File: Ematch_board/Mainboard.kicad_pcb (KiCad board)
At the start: 4 copper layers, 57 x 53 mm, 124 parts, among them J1 Conn_01x02_Male, J10 Conn_01x02_Male, J11 Conn_Coaxial, J2 Conn_01x02_Male, J3 Conn_01x02_Male, J4 Conn_01x02_Male, J5 Conn_01x02_Male, J6 Conn_01x02_Male, J7 RBUS, J8 USB_C_Receptacle_USB2.0, J9 Conn_01x02_Male, Q1 MMDT2222A, Q51 PMV20ENR, Q52 PMV20ENR, Q53 PMV20ENR, Q54 PMV20ENR, Q55 PMV20ENR, Q56 PMV20ENR, U1 LTV-247, U2 LTC4411, U3 SC4216H, U4 LTC4411, U5 SN65HVD230, U6 CP2102-GMR-QFN28

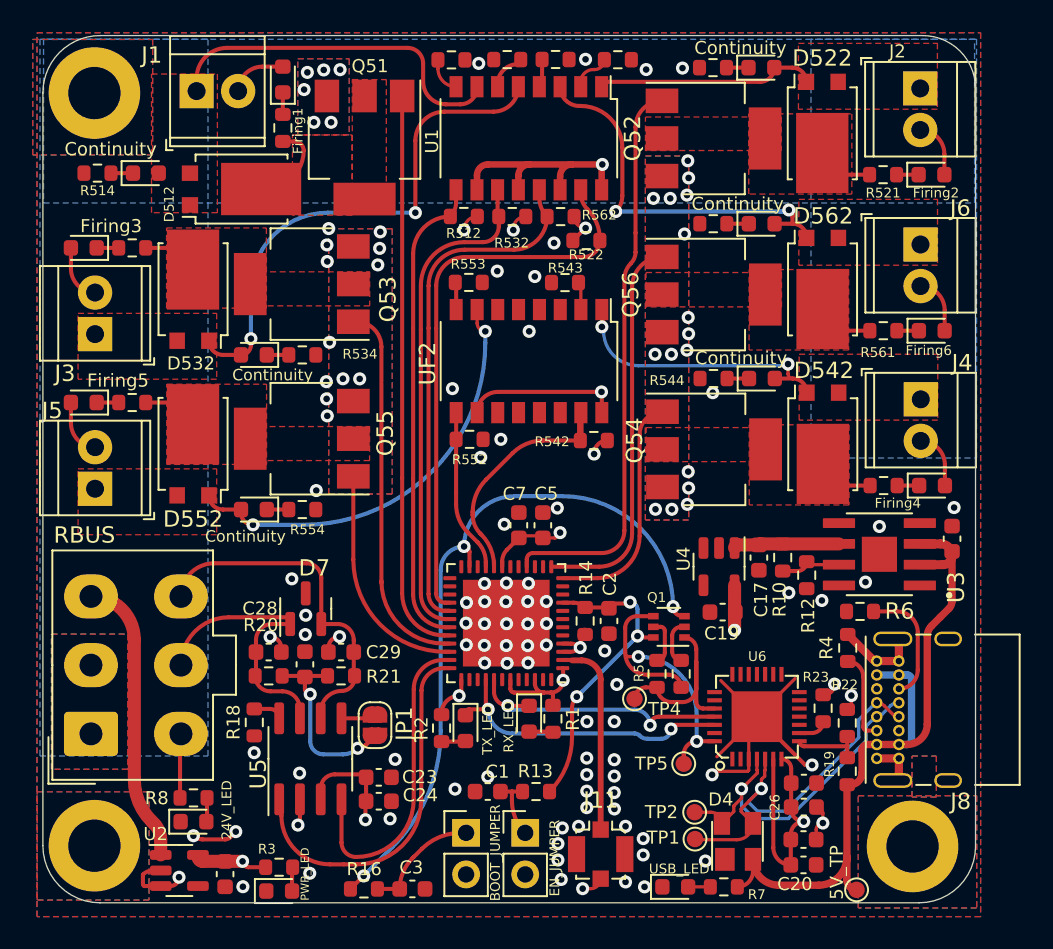
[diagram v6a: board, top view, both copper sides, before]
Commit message: Changed ESP32 pin assignment from special IO pins
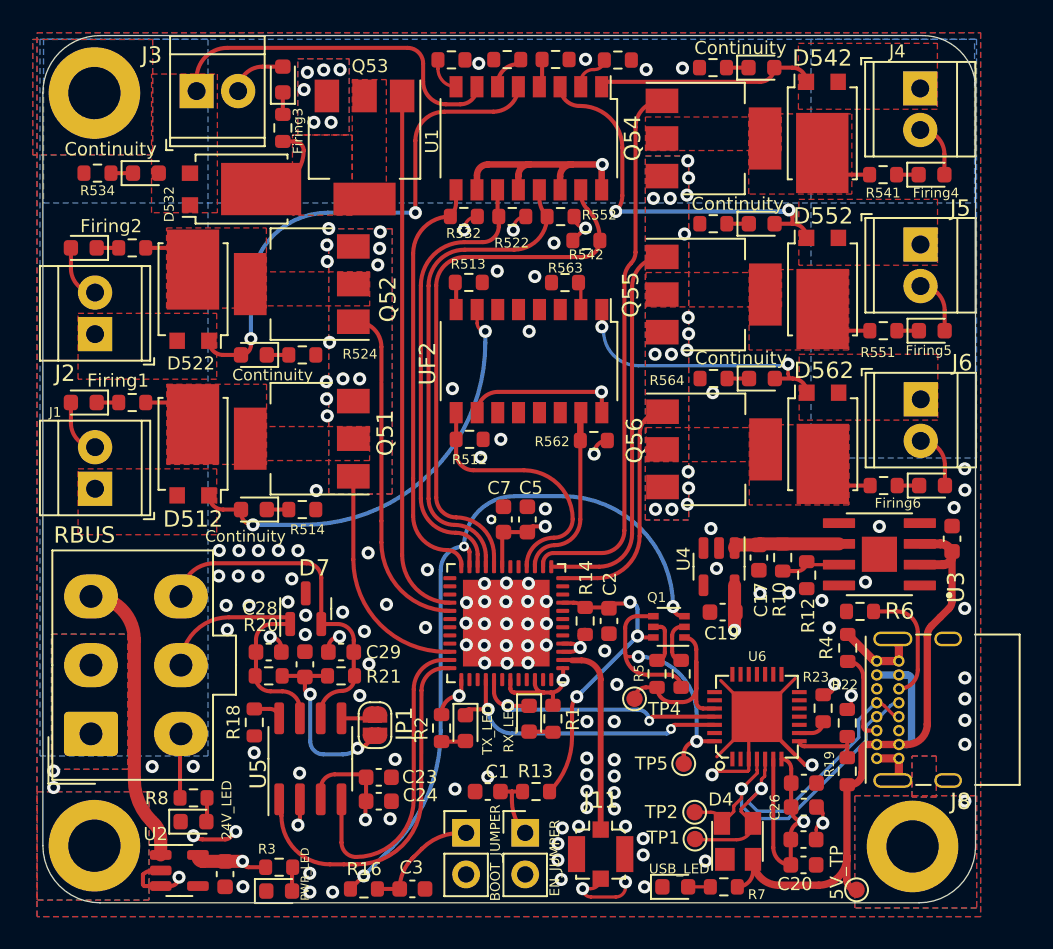
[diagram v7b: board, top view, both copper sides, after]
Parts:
- Firing1: renamed from Firing5; value D551 -> D511
- Firing2: renamed from Firing3; value D531 -> D521
- Firing3: renamed from Firing1; value D511 -> D531
- Firing4: renamed from Firing2; value D521 -> D541
- Firing5: renamed from Firing6; value D561 -> D551
- Firing6: renamed from Firing4; value D541 -> D561
- R513: renamed from R553; value 1k -> 10k
- R523: renamed from R533; value 1k -> 10k
- R533: renamed from R513; value 1k -> 10k
- R543: renamed from R523; value 1k -> 10k
- R553: renamed from R563; value 1k -> 10k
- R563: renamed from R543; value 1k -> 10k
- moved C5 1.01 mm to (147.8, 99.0)
- moved C7 1.01 mm to (146.3, 99.0)
- renumbered D552 to D512, D553 to D513, D532 to D522, D533 to D523, D512 to D532, D513 to D533, D522 to D542, D523 to D543, D562 to D552, D563 to D553, D542 to D562, D543 to D563, J5 to J1, J3 to J2, J1 to J3, J2 to J4, J6 to J5, J4 to J6, Q55 to Q51, Q53 to Q52, Q51 to Q53, Q52 to Q54, Q56 to Q55, Q54 to Q56, R551 to R511, R552 to R512, R554 to R514, R531 to R521, R532 to R522, R534 to R524, R511 to R531, R512 to R532, R514 to R534, R521 to R541, R522 to R542, R524 to R544, R561 to R551, R562 to R552, R564 to R554, R541 to R561, R542 to R562, R544 to R564
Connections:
- GND1 pad 12: /Nuke 4 -> /Nuke 6
- GND1 pad 13: /Nuke 6 -> /Nuke 5
- GND1 pad 14: unconnected-(GND1-Pad14) -> /Nuke 4
- GND1 pad 15: unconnected-(GND1-Pad15) -> /Cont 6
- GND1 pad 16: /Nuke 2 -> /Cont 1
- GND1 pad 22: unconnected-(GND1-Pad22) -> /Cont 2
- GND1 pad 24: unconnected-(GND1-Pad24) -> /Cont 3
- GND1 pad 28: /Cont 2 -> /Nuke 3
- GND1 pad 29: /Cont 6 -> /Nuke 2
- GND1 pad 30: /Cont 3 -> unconnected-(GND1-Pad30)
- GND1 pad 31: /Cont 1 -> unconnected-(GND1-Pad31)
- GND1 pad 32: /Nuke 1 -> unconnected-(GND1-Pad32)
- GND1 pad 33: /Nuke 3 -> unconnected-(GND1-Pad33)
- GND1 pad 34: /Nuke 5 -> /Nuke 1
- Q51 pad 1: /Nuke 5 -> /Nuke 1
- Q52 pad 1: /Nuke 3 -> /Nuke 2
- Q53 pad 1: /Nuke 1 -> /Nuke 3
- Q54 pad 1: /Nuke 2 -> /Nuke 4
- Q55 pad 1: /Nuke 6 -> /Nuke 5
- Q56 pad 1: /Nuke 4 -> /Nuke 6
- R512 pad 1: /Cont 5 -> /Cont 1
- R522 pad 1: /Cont 3 -> /Cont 2
- R532 pad 1: /Cont 1 -> /Cont 3
- R542 pad 1: /Cont 2 -> /Cont 4
- R552 pad 1: /Cont 6 -> /Cont 5
- R562 pad 1: /Cont 4 -> /Cont 6
- U1 pad 11: /Cont 3 -> /Cont 2
- U1 pad 13: /Cont 6 -> /Cont 5
- U1 pad 15: /Cont 2 -> /Cont 4
- U1 pad 9: /Cont 1 -> /Cont 3
- UF2 pad 15: /Cont 4 -> /Cont 6
- UF2 pad 9: /Cont 5 -> /Cont 1
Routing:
- net /Cont 6: track 32.3 -> 10.9 mm
- net /Nuke 1: track 34.7 -> 14.0 mm
- net /Cont 5: track 9.97 -> 30.3 mm
- net /Cont 4: track 14.4 -> 33.9 mm
- net /Nuke 4: track 14.4 -> 33.5 mm
- net /Nuke 2: track 34.6 -> 20.8 mm
- net /Cont 1: track 29.3 -> 16.1 mm
- net /Nuke 5: track 14.0 -> 23.9 mm
- net /Nuke 6: track 23.9 -> 14.4 mm
- net /Nuke 3: track 23.1 -> 32.5 mm
- net /Cont 2: track 34.8 -> 27.9 mm
- net /Cont 3: track 30.4 -> 25.9 mm
- net GND: track 50.7 -> 54.2 mm, vias 124 -> 162
- net +3V3: track 72.4 -> 71.7 mm
